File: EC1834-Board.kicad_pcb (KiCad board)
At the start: 2 copper layers, 18 parts

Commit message: Page 1 & 2 connected Hierarchival connections created and tested
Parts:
- moved REF** 103.7 mm to (22.2, -75.7)
- moved REF** 103.7 mm to (108.6, -47.8)
- moved REF** 103.7 mm to (54.6, -47.8)
- moved REF** 103.7 mm to (43.8, -47.8)
- moved REF** 103.7 mm to (22.2, -47.8)
- moved REF** 103.7 mm to (65.4, -47.8)
- moved REF** 103.7 mm to (87.0, -47.8)
- moved REF** 103.7 mm to (97.8, -47.8)
- moved REF** 103.7 mm to (33.0, -47.8)
- moved REF** 103.7 mm to (76.2, -47.8)
- moved REF** 103.7 mm to (33.0, -75.7)
- moved REF** 103.7 mm to (43.8, -75.7)
- moved REF** 103.7 mm to (54.6, -75.7)
- moved REF** 103.7 mm to (97.8, -75.7)
- moved REF** 103.7 mm to (87.0, -75.7)
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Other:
- board outline added: 360 x 240 mm
- copper layers 2 -> 6
- net class Default removed

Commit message: Updated footprint for EMR UC8821 Added footprint for PS5 PCB layout in progress small corrections in schematics
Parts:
- added BR1: SolderJumper_2_Bridged, Resistor_THT:R_Axial_DIN0204_L3.6mm_D1.6mm_P7.62mm_Horizontal, F.Cu at (259.1, -55.9)
- added Br2: Br2, Resistor_THT:R_Axial_DIN0204_L3.6mm_D1.6mm_P7.62mm_Horizontal, F.Cu at (362.2, -28.5)
- added Br3: Br3, Resistor_THT:R_Axial_DIN0204_L3.6mm_D1.6mm_P7.62mm_Horizontal, F.Cu at (362.2, -31.7)
- added Br4: Br4, Resistor_THT:R_Axial_DIN0204_L3.6mm_D1.6mm_P5.08mm_Horizontal, F.Cu at (251.4, -191.6)
- added C10: 10pF, Capacitor_THT:C_Disc_D4.3mm_W1.9mm_P5.00mm, F.Cu at (184.2, -131.2)
- added C101: 47µF, Capacitor_THT:CP_Radial_D12.5mm_P5.00mm, F.Cu at (521.1, -90.7)
- added C102: 47µF, Capacitor_THT:CP_Radial_D12.5mm_P5.00mm, F.Cu at (564.3, -79.0)
- added C103: 47µF, Capacitor_THT:CP_Radial_D12.5mm_P5.00mm, F.Cu at (536.9, -95.4)
- added C104: 47µF, Capacitor_THT:CP_Radial_D12.5mm_P5.00mm, F.Cu at (551.3, -95.4)
- added C105: 47µF, Capacitor_THT:CP_Radial_D12.5mm_P5.00mm, F.Cu at (608.4, -121.2)
- added C106: 47µF, Capacitor_THT:CP_Radial_D12.5mm_P5.00mm, F.Cu at (594.0, -121.2)
- added C107: 47µF, Capacitor_THT:CP_Radial_D12.5mm_P5.00mm, F.Cu at (535.5, -67.3)
- added C108: 47µF, Capacitor_THT:CP_Radial_D12.5mm_P5.00mm, F.Cu at (594.5, -93.1)
- added C109: 47µF, Capacitor_THT:CP_Radial_D12.5mm_P5.00mm, F.Cu at (580.1, -93.1)
- added C110: 47µF, Capacitor_THT:CP_Radial_D12.5mm_P5.00mm, F.Cu at (593.1, -79.0)
- added C111: 47µF, Capacitor_THT:CP_Radial_D12.5mm_P5.00mm, F.Cu at (598.3, -107.1)
- added C112: 47µF, Capacitor_THT:CP_Radial_D12.5mm_P5.00mm, F.Cu at (637.2, -121.2)
- added C113: 47µF, Capacitor_THT:CP_Radial_D12.5mm_P5.00mm, F.Cu at (578.7, -79.0)
- added C114: 47µF, Capacitor_THT:CP_Radial_D12.5mm_P5.00mm, F.Cu at (583.9, -107.1)
- added C115: 47µF, Capacitor_THT:CP_Radial_D12.5mm_P5.00mm, F.Cu at (549.9, -67.3)
- added C116: 47µF, Capacitor_THT:CP_Radial_D12.5mm_P5.00mm, F.Cu at (579.6, -121.2)
- added C117: 47µF, Capacitor_THT:CP_Radial_D12.5mm_P5.00mm, F.Cu at (578.7, -65.0)
- added C118: 47µF, Capacitor_THT:CP_Radial_D12.5mm_P5.00mm, F.Cu at (549.9, -81.4)
- added C119: 47µF, Capacitor_THT:CP_Radial_D12.5mm_P5.00mm, F.Cu at (565.7, -93.1)
- added C120: 47µF, Capacitor_THT:CP_Radial_D12.5mm_P5.00mm, F.Cu at (521.1, -62.6)
- added C121: 47µF, Capacitor_THT:CP_Radial_D12.5mm_P5.00mm, F.Cu at (535.5, -81.4)
- added C122: 47µF, Capacitor_THT:CP_Radial_D12.5mm_P5.00mm, F.Cu at (564.3, -65.0)
- added C123: 47µF, Capacitor_THT:CP_Radial_D12.5mm_P5.00mm, F.Cu at (569.5, -107.1)
- added C2: 47µF, Capacitor_THT:CP_Radial_D12.5mm_P5.00mm, F.Cu at (622.8, -121.2)
- added C3: 47µF, Capacitor_THT:CP_Radial_D12.5mm_P5.00mm, F.Cu at (342.3, 231.8)
- added C4: 47µF, Capacitor_THT:CP_Radial_D12.5mm_P5.00mm, F.Cu at (521.1, -76.6)
- added C5: 47µF, Capacitor_THT:CP_Radial_D12.5mm_P5.00mm, F.Cu at (286.4, -149.8)
- added C6: 10nF, Capacitor_THT:C_Disc_D4.3mm_W1.9mm_P5.00mm, F.Cu at (185.4, -145.8)
- added C7: 680pF, Capacitor_THT:C_Disc_D4.3mm_W1.9mm_P5.00mm, F.Cu at (266.7, -87.0)
- added C8: 680pF, Capacitor_THT:C_Disc_D4.3mm_W1.9mm_P5.00mm, F.Cu at (221.7, -30.8)
- added D1: K1810WM87, Package_DIP:DIP-40_W15.24mm, F.Cu at (347.3, 208.3)
- added D10: DL000D, Package_DIP:DIP-14_W7.62mm, F.Cu at (170.4, 219.1)
- added D100: U2764, Package_DIP:DIP-28_W15.24mm, F.Cu at (185.4, 31.1)
- added D101: U2764, Package_DIP:DIP-28_W15.24mm, F.Cu at (144.8, 31.1)
- added D102: U2164, Package_DIP:DIP-16_W7.62mm, F.Cu at (106.7, 55.2)
- added D103: U2164, Package_DIP:DIP-16_W7.62mm, F.Cu at (96.5, 55.2)
- added D104: U2164, Package_DIP:DIP-16_W7.62mm, F.Cu at (86.3, 55.2)
- added D105: U2164, Package_DIP:DIP-16_W7.62mm, F.Cu at (76.2, 55.2)
- added D106: U2164, Package_DIP:DIP-16_W7.62mm, F.Cu at (66.0, 55.2)
- added D107: U2164, Package_DIP:DIP-16_W7.62mm, F.Cu at (55.9, 55.2)
- added D108: U2164, Package_DIP:DIP-16_W7.62mm, F.Cu at (45.7, 55.2)
- added D109: U2164, Package_DIP:DIP-16_W7.62mm, F.Cu at (35.5, 55.2)
- added D11: DL020D, Package_DIP:DIP-14_W7.62mm, F.Cu at (158.3, 219.1)
- added D110: U2164, Package_DIP:DIP-16_W7.62mm, F.Cu at (25.4, 55.2)
- added D111: DS8286D-D111, Package_DIP:DIP-20_W7.62mm, F.Cu at (244.5, 33.6)
- added D112: DS8286D-D111, Package_DIP:DIP-20_W7.62mm, F.Cu at (229.9, 33.7)
- added D113: KR531IP5, Package_DIP:DIP-14_W7.62mm, F.Cu at (215.3, 33.7)
- added D114: KR531IP5, Package_DIP:DIP-14_W7.62mm, F.Cu at (202.6, 33.7)
- added D115: U2764, Package_DIP:DIP-28_W15.24mm, F.Cu at (185.4, 10.8)
- added D116: U2764, Package_DIP:DIP-28_W15.24mm, F.Cu at (144.8, 10.8)
- added D117: U2164, Package_DIP:DIP-16_W7.62mm, F.Cu at (106.7, 28.6)
- added D118: U2164, Package_DIP:DIP-16_W7.62mm, F.Cu at (96.5, 28.6)
- added D119: U2164, Package_DIP:DIP-16_W7.62mm, F.Cu at (86.3, 28.6)
- added D12: DL008D, Package_DIP:DIP-14_W7.62mm, F.Cu at (146.3, 219.1)
- added D120: U2164, Package_DIP:DIP-16_W7.62mm, F.Cu at (76.2, 28.6)
- added D121: U2164, Package_DIP:DIP-16_W7.62mm, F.Cu at (66.0, 28.6)
- added D122: U2164, Package_DIP:DIP-16_W7.62mm, F.Cu at (55.9, 28.6)
- added D123: U2164, Package_DIP:DIP-16_W7.62mm, F.Cu at (45.7, 28.6)
- added D124: U2164, Package_DIP:DIP-16_W7.62mm, F.Cu at (35.5, 28.6)
- added D125: U2164, Package_DIP:DIP-16_W7.62mm, F.Cu at (25.4, 28.6)
- added D126: DL074, Package_DIP:DIP-14_W7.62mm, F.Cu at (354.3, 64.1)
- added D13: DL074, Package_DIP:DIP-14_W7.62mm, F.Cu at (134.2, 219.1)
- added D14: DL010D, Package_DIP:DIP-14_W7.62mm, F.Cu at (119.6, 219.1)
- added D15: DL074, Package_DIP:DIP-14_W7.62mm, F.Cu at (105.0, 219.1)
- added D16: DL000D, Package_DIP:DIP-14_W7.62mm, F.Cu at (89.5, 219.1)
- added D2: DS8282, Package_DIP:DIP-20_W7.62mm, F.Cu at (285.1, 218.4)
- added D20: K1810WM86, Package_DIP:DIP-40_W15.24mm, F.Cu at (342.3, 188.0)
- added D21: DS8286D-D111, Package_DIP:DIP-20_W7.62mm, F.Cu at (339.7, 182.9)
- added D22: DS8286D, Package_DIP:DIP-20_W7.62mm, F.Cu at (327.0, 182.9)
- added D23: DS8286D-D23, Package_DIP:DIP-20_W7.62mm, F.Cu at (314.3, 182.9)
- added D24: DL374, Package_DIP:DIP-20_W7.62mm, F.Cu at (301.6, 182.9)
- added D25: DS8282, Package_DIP:DIP-20_W7.62mm, F.Cu at (285.1, 185.4)
- added D26: DS8282, Package_DIP:DIP-20_W7.62mm, F.Cu at (272.4, 185.4)
- added D27: DS8286D-D27, Package_DIP:DIP-20_W7.62mm, F.Cu at (244.5, 185.2)
- added D28: DL295, Package_DIP:DIP-14_W7.62mm, F.Cu at (228.0, 198.2)
- added D29: DL295, Package_DIP:DIP-14_W7.62mm, F.Cu at (228.0, 177.9)
- added D3: DL020D, Package_DIP:DIP-14_W7.62mm, F.Cu at (272.4, 218.4)
- added D30: DL374, Package_DIP:DIP-20_W7.62mm, F.Cu at (215.3, 185.5)
- added D31: DL374, Package_DIP:DIP-20_W7.62mm, F.Cu at (202.6, 185.5)
- added D32: DL000D, Package_DIP:DIP-14_W7.62mm, F.Cu at (182.5, 193.7)
- added D33: DL002D, Package_DIP:DIP-14_W7.62mm, F.Cu at (170.2, 193.7)
- added D34: DL004D, Package_DIP:DIP-14_W7.62mm, F.Cu at (158.1, 193.7)
- added D35: DL175, Package_DIP:DIP-16_W7.62mm, F.Cu at (146.1, 193.7)
- added D36: DL175, Package_DIP:DIP-16_W7.62mm, F.Cu at (134.0, 193.7)
- added D37: DL032D, Package_DIP:DIP-14_W7.62mm, F.Cu at (119.4, 193.7)
- added D38: DL074, Package_DIP:DIP-14_W7.62mm, F.Cu at (104.8, 193.7)
- added D39: DL000D, Package_DIP:DIP-14_W7.62mm, F.Cu at (89.5, 193.7)
- added D4: KR1810WG88, Package_DIP:DIP-20_W7.62mm, F.Cu at (259.7, 218.4)
- added D40: DL008D, Package_DIP:DIP-14_W7.62mm, F.Cu at (74.9, 193.7)
- added D42: A302D, Package_DIP:DIP-4_W7.62mm, F.Cu at (185.5, -165.0)
- added D43: 8284, Package_DIP:DIP-18_W7.62mm, F.Cu at (356.9, 139.7)
- added D44: DS8286D-D111, Package_DIP:DIP-20_W7.62mm, F.Cu at (244.5, 151.1)
- added D45: DS8282, Package_DIP:DIP-20_W7.62mm, F.Cu at (228.0, 151.1)
- added D46: DS8216, Package_DIP:DIP-16_W7.62mm, F.Cu at (215.3, 146.0)
- added D47: DL008D, Package_DIP:DIP-14_W7.62mm, F.Cu at (202.6, 143.5)
- added D48: KR580WN59A, Package_DIP:DIP-28_W15.24mm, F.Cu at (185.4, 165.1)
- added D49: KR580WN59A, Package_DIP:DIP-28_W15.24mm, F.Cu at (165.7, 165.1)
- added D5: DL030D, Package_DIP:DIP-14_W7.62mm, F.Cu at (244.5, 218.4)
- added D50: KR580IK57, Package_DIP:DIP-40_W15.24mm, F.Cu at (146.0, 165.1)
- added D51: DL074, Package_DIP:DIP-14_W7.62mm, F.Cu at (121.9, 165.1)
- added D52: 74HC74, Package_DIP:DIP-14_W7.62mm, F.Cu at (121.9, 139.7)
- added D53: KR580WI53, Package_DIP:DIP-24_W15.24mm, F.Cu at (106.7, 144.8)
- added D54: 8255A, Package_DIP:DIP-40_W15.24mm, F.Cu at (83.2, 165.1)
- added D55: UC8821, EC1834-Board:EMR-64_W22.86mm, F.Cu at (61.0, 156.2)
- added D56: 2716, Package_DIP:DIP-24_W15.24mm, F.Cu at (30.5, 147.3)
- added D57: DL008D, Package_DIP:DIP-14_W7.62mm, F.Cu at (244.5, 123.2)
- added D58: 74HC74, Package_DIP:DIP-14_W7.62mm, F.Cu at (228.0, 123.2)
- added D59: DL004D, Package_DIP:DIP-14_W7.62mm, F.Cu at (215.3, 123.2)
- added D6: DL295, Package_DIP:DIP-14_W7.62mm, F.Cu at (228.0, 218.4)
- added D60: 74HC74, Package_DIP:DIP-14_W7.62mm, F.Cu at (202.6, 123.2)
- added D61: DS8216, Package_DIP:DIP-16_W7.62mm, F.Cu at (185.4, 123.2)
- added D62: DL032D, Package_DIP:DIP-14_W7.62mm, F.Cu at (173.4, 123.2)
- added D63: DL010D-D63, Package_DIP:DIP-14_W7.62mm, F.Cu at (160.0, 123.2)
- added D64: DS8286D-D23, Package_DIP:DIP-20_W7.62mm, F.Cu at (244.5, 99.0)
- added D65: DS8205, Package_DIP:DIP-16_W7.62mm, F.Cu at (228.0, 99.0)
- added D66: DS8205, Package_DIP:DIP-16_W7.62mm, F.Cu at (215.3, 99.0)
- added D67: DL074, Package_DIP:DIP-14_W7.62mm, F.Cu at (202.6, 99.1)
- added D68: 74S51, Package_DIP:DIP-14_W7.62mm, F.Cu at (185.4, 99.1)
- added D69: DL008D, Package_DIP:DIP-14_W7.62mm, F.Cu at (173.3, 99.1)
- added D7: DL032D, Package_DIP:DIP-14_W7.62mm, F.Cu at (215.2, 218.4)
- added D70: DL008D, Package_DIP:DIP-14_W7.62mm, F.Cu at (160.0, 99.1)
- added D71: DL002D, Package_DIP:DIP-14_W7.62mm, F.Cu at (138.4, 106.7)
- added D72: DL008D, Package_DIP:DIP-14_W7.62mm, F.Cu at (121.9, 109.2)
- added D73: U2164, Package_DIP:DIP-16_W7.62mm, F.Cu at (106.7, 107.9)
- added D74: U2164, Package_DIP:DIP-16_W7.62mm, F.Cu at (96.5, 107.9)
- added D75: U2164, Package_DIP:DIP-16_W7.62mm, F.Cu at (86.3, 107.9)
- added D76: U2164, Package_DIP:DIP-16_W7.62mm, F.Cu at (76.2, 107.9)
- added D77: U2164, Package_DIP:DIP-16_W7.62mm, F.Cu at (66.0, 107.9)
- added D78: U2164, Package_DIP:DIP-16_W7.62mm, F.Cu at (55.9, 107.9)
- added D79: U2164, Package_DIP:DIP-16_W7.62mm, F.Cu at (45.7, 107.9)
- added D8: DL004D, Package_DIP:DIP-14_W7.62mm, F.Cu at (202.5, 218.4)
- added D80: U2164, Package_DIP:DIP-16_W7.62mm, F.Cu at (35.5, 107.9)
- added D81: U2164, Package_DIP:DIP-16_W7.62mm, F.Cu at (25.4, 107.9)
- added D82: DL004D, Package_DIP:DIP-14_W7.62mm, F.Cu at (11.4, 99.7)
- added D83: DS8286D, Package_DIP:DIP-20_W7.62mm, F.Cu at (244.5, 66.7)
- added D84: DS8286D, Package_DIP:DIP-20_W7.62mm, F.Cu at (228.0, 66.7)
- added D85: KR531KP11, Package_DIP:DIP-16_W7.62mm, F.Cu at (215.3, 61.6)
- added D86: KR531KP11, Package_DIP:DIP-16_W7.62mm, F.Cu at (202.6, 61.6)
- added D87: DL004D, Package_DIP:DIP-14_W7.62mm, F.Cu at (173.3, 73.0)
- added D88: DL008D, Package_DIP:DIP-14_W7.62mm, F.Cu at (160.0, 73.0)
- added D89: DS8205, Package_DIP:DIP-16_W7.62mm, F.Cu at (138.4, 73.0)
- added D9: DS8205, Package_DIP:DIP-16_W7.62mm, F.Cu at (182.5, 219.1)
- added D90: KR531LI1, Package_DIP:DIP-14_W7.62mm, F.Cu at (123.8, 73.0)
- added D91: U2164, Package_DIP:DIP-16_W7.62mm, F.Cu at (106.7, 81.9)
- added D92: U2164, Package_DIP:DIP-16_W7.62mm, F.Cu at (96.5, 81.9)
- added D93: U2164, Package_DIP:DIP-16_W7.62mm, F.Cu at (86.3, 81.9)
- added D94: U2164, Package_DIP:DIP-16_W7.62mm, F.Cu at (76.2, 81.9)
- added D95: U2164, Package_DIP:DIP-16_W7.62mm, F.Cu at (66.0, 81.9)
- added D96: U2164, Package_DIP:DIP-16_W7.62mm, F.Cu at (55.9, 81.9)
- added D97: U2164, Package_DIP:DIP-16_W7.62mm, F.Cu at (45.7, 81.9)
- added D98: U2164, Package_DIP:DIP-16_W7.62mm, F.Cu at (35.5, 81.9)
- added D99: U2164, Package_DIP:DIP-16_W7.62mm, F.Cu at (25.4, 81.9)
- added E1: SolderJumper_2_Bridged, Connector_PinHeader_2.54mm:PinHeader_1x02_P2.54mm_Vertical, F.Cu at (284.8, -239.8)
- added E2: SolderJumper_2_Bridged, Connector_PinHeader_2.54mm:PinHeader_1x02_P2.54mm_Vertical, F.Cu at (343.7, -215.2)
- added E4: SolderJumper_2_Bridged, Connector_PinHeader_2.54mm:PinHeader_1x02_P2.54mm_Vertical, F.Cu at (44.5, 167.0)
- added E5: SolderJumper_2_Bridged, Connector_PinHeader_2.54mm:PinHeader_1x02_P2.54mm_Vertical, F.Cu at (284.8, -232.6)
- added E6: Conn_01x02, Connector_PinHeader_2.54mm:PinHeader_1x02_P2.54mm_Vertical, F.Cu at (649.0, -111.5)
- added E7: Conn_01x02, Connector_PinHeader_2.54mm:PinHeader_1x02_P2.54mm_Vertical, F.Cu at (649.0, -104.3)
- added E8: Conn_01x02, Connector_PinHeader_2.54mm:PinHeader_1x02_P2.54mm_Vertical, F.Cu at (649.1, -118.7)
- added K1: 100n, Capacitor_THT:C_Disc_D4.3mm_W1.9mm_P5.00mm, F.Cu at (638.2, -95.2)
- added K10: 100n, Capacitor_THT:C_Disc_D4.3mm_W1.9mm_P5.00mm, F.Cu at (583.0, -56.2)
- added K100: 100n, Capacitor_THT:C_Disc_D4.3mm_W1.9mm_P5.00mm, F.Cu at (525.9, -50.4)
- added K101: 100n, Capacitor_THT:C_Disc_D4.3mm_W1.9mm_P5.00mm, F.Cu at (534.1, -55.1)
- added K102: 100n, Capacitor_THT:C_Disc_D4.3mm_W1.9mm_P5.00mm, F.Cu at (607.4, -53.3)
- added K103: 100n, Capacitor_THT:C_Disc_D4.3mm_W1.9mm_P5.00mm, F.Cu at (628.6, -74.5)
- added K104: 100n, Capacitor_THT:C_Disc_D4.3mm_W1.9mm_P5.00mm, F.Cu at (589.8, -66.8)
- added K105: 100n, Capacitor_THT:C_Disc_D4.3mm_W1.9mm_P5.00mm, F.Cu at (615.6, -57.0)
- added K106: 100n, Capacitor_THT:C_Disc_D4.3mm_W1.9mm_P5.00mm, F.Cu at (607.4, -49.8)
- added K107: 100n, Capacitor_THT:C_Disc_D4.3mm_W1.9mm_P5.00mm, F.Cu at (636.8, -81.4)
- added K108: 100n, Capacitor_THT:C_Disc_D4.3mm_W1.9mm_P5.00mm, F.Cu at (622.4, -63.9)
- added K109: 100n, Capacitor_THT:C_Disc_D4.3mm_W1.9mm_P5.00mm, F.Cu at (630.5, -71.0)
- added K11: 100n, Capacitor_THT:C_Disc_D4.3mm_W1.9mm_P5.00mm, F.Cu at (605.6, -94.9)
- added K110: 100n, Capacitor_THT:C_Disc_D4.3mm_W1.9mm_P5.00mm, F.Cu at (636.8, -77.9)
- added K111: 100n, Capacitor_THT:C_Disc_D4.3mm_W1.9mm_P5.00mm, F.Cu at (591.1, -53.0)
- added K112: 100n, Capacitor_THT:C_Disc_D4.3mm_W1.9mm_P5.00mm, F.Cu at (612.3, -74.2)
- added K113: 100n, Capacitor_THT:C_Disc_D4.3mm_W1.9mm_P5.00mm, F.Cu at (534.1, -51.7)
- added K114: 100n, Capacitor_THT:C_Disc_D4.3mm_W1.9mm_P5.00mm, F.Cu at (534.1, -48.2)
- added K115: 100n, Capacitor_THT:C_Disc_D4.3mm_W1.9mm_P5.00mm, F.Cu at (540.3, -58.6)
- added K116: 100n, Capacitor_THT:C_Disc_D4.3mm_W1.9mm_P5.00mm, F.Cu at (542.2, -55.1)
- added K117: 100n, Capacitor_THT:C_Disc_D4.3mm_W1.9mm_P5.00mm, F.Cu at (615.6, -53.5)
- added K118: 100n, Capacitor_THT:C_Disc_D4.3mm_W1.9mm_P5.00mm, F.Cu at (636.8, -74.5)
- added K119: 100n, Capacitor_THT:C_Disc_D4.3mm_W1.9mm_P5.00mm, F.Cu at (623.7, -57.0)
- added K12: 100n, Capacitor_THT:C_Disc_D4.3mm_W1.9mm_P5.00mm, F.Cu at (631.9, -109.0)
- added K120: 100n, Capacitor_THT:C_Disc_D4.3mm_W1.9mm_P5.00mm, F.Cu at (615.6, -50.1)
- added K121: 100n, Capacitor_THT:C_Disc_D4.3mm_W1.9mm_P5.00mm, F.Cu at (630.5, -67.6)
- added K122: 100n, Capacitor_THT:C_Disc_D4.3mm_W1.9mm_P5.00mm, F.Cu at (542.2, -51.7)
- added K123: 100n, Capacitor_THT:C_Disc_D4.3mm_W1.9mm_P5.00mm, F.Cu at (548.5, -58.6)
- added K124: 100n, Capacitor_THT:C_Disc_D4.3mm_W1.9mm_P5.00mm, F.Cu at (542.2, -48.2)
- added K125: 100n, Capacitor_THT:C_Disc_D4.3mm_W1.9mm_P5.00mm, F.Cu at (550.4, -55.1)
- added K126: 100n, Capacitor_THT:C_Disc_D4.3mm_W1.9mm_P5.00mm, F.Cu at (589.8, -59.9)
- added K13: 100n, Capacitor_THT:C_Disc_D4.3mm_W1.9mm_P5.00mm, F.Cu at (640.1, -112.4)
- added K14: 100n, Capacitor_THT:C_Disc_D4.3mm_W1.9mm_P5.00mm, F.Cu at (591.1, -56.5)
- added K15: 100n, Capacitor_THT:C_Disc_D4.3mm_W1.9mm_P5.00mm, F.Cu at (621.9, -95.2)
- added K16: 100n, Capacitor_THT:C_Disc_D4.3mm_W1.9mm_P5.00mm, F.Cu at (574.8, -49.3)
- added K18: 100n, Capacitor_THT:C_Disc_D4.3mm_W1.9mm_P5.00mm, F.Cu at (622.4, -67.3)
- added K19: 100n, Capacitor_THT:C_Disc_D4.3mm_W1.9mm_P5.00mm, F.Cu at (622.4, -60.4)
- added K2: 100n, Capacitor_THT:C_Disc_D4.3mm_W1.9mm_P5.00mm, F.Cu at (280.7, 223.5)
- added K21: 100n, Capacitor_THT:C_Disc_D4.3mm_W1.9mm_P5.00mm, F.Cu at (583.0, -49.3)
- added K22: 100n, Capacitor_THT:C_Disc_D4.3mm_W1.9mm_P5.00mm, F.Cu at (631.9, -98.6)
- added K23: 100n, Capacitor_THT:C_Disc_D4.3mm_W1.9mm_P5.00mm, F.Cu at (640.1, -109.0)
- added K24: 100n, Capacitor_THT:C_Disc_D4.3mm_W1.9mm_P5.00mm, F.Cu at (597.9, -66.8)
- added K25: 100n, Capacitor_THT:C_Disc_D4.3mm_W1.9mm_P5.00mm, F.Cu at (278.1, 190.5)
- added K26: 100n, Capacitor_THT:C_Disc_D4.3mm_W1.9mm_P5.00mm, F.Cu at (550.4, -48.2)
- added K27: 100n, Capacitor_THT:C_Disc_D4.3mm_W1.9mm_P5.00mm, F.Cu at (606.1, -70.5)
- added K28: 100n, Capacitor_THT:C_Disc_D4.3mm_W1.9mm_P5.00mm, F.Cu at (574.8, -56.2)
- added K29: 100n, Capacitor_THT:C_Disc_D4.3mm_W1.9mm_P5.00mm, F.Cu at (623.8, -109.0)
- added K3: 100n, Capacitor_THT:C_Disc_D4.3mm_W1.9mm_P5.00mm, F.Cu at (605.6, -98.4)
- added K30: 100n, Capacitor_THT:C_Disc_D4.3mm_W1.9mm_P5.00mm, F.Cu at (212.6, 190.5)
- added K31: 100n, Capacitor_THT:C_Disc_D4.3mm_W1.9mm_P5.00mm, F.Cu at (199.9, 190.5)
- added K32: 100n, Capacitor_THT:C_Disc_D4.3mm_W1.9mm_P5.00mm, F.Cu at (670.6, -94.0)
- added K33: 100n, Capacitor_THT:C_Disc_D4.3mm_W1.9mm_P5.00mm, F.Cu at (597.9, -63.4)
- added K34: 100n, Capacitor_THT:C_Disc_D4.3mm_W1.9mm_P5.00mm, F.Cu at (605.6, -91.5)
- added K35: 100n, Capacitor_THT:C_Disc_D4.3mm_W1.9mm_P5.00mm, F.Cu at (630.1, -95.2)
- added K36: 100n, Capacitor_THT:C_Disc_D4.3mm_W1.9mm_P5.00mm, F.Cu at (620.5, -84.6)
- added K37: 100n, Capacitor_THT:C_Disc_D4.3mm_W1.9mm_P5.00mm, F.Cu at (566.7, -52.8)
- added K38: 100n, Capacitor_THT:C_Disc_D4.3mm_W1.9mm_P5.00mm, F.Cu at (612.3, -84.6)
- added K39: 100n, Capacitor_THT:C_Disc_D4.3mm_W1.9mm_P5.00mm, F.Cu at (604.2, -80.9)
- added K4: 100n, Capacitor_THT:C_Disc_D4.3mm_W1.9mm_P5.00mm, F.Cu at (558.5, -49.3)
- added K40: 100n, Capacitor_THT:C_Disc_D4.3mm_W1.9mm_P5.00mm, F.Cu at (613.8, -91.5)
- added K43: 100n, Capacitor_THT:C_Disc_D4.3mm_W1.9mm_P5.00mm, F.Cu at (630.1, -91.7)
- added K44: 100n, Capacitor_THT:C_Disc_D4.3mm_W1.9mm_P5.00mm, F.Cu at (238.1, 156.2)
- added K45: 100n, Capacitor_THT:C_Disc_D4.3mm_W1.9mm_P5.00mm, F.Cu at (558.5, -52.8)
- added K46: 100n, Capacitor_THT:C_Disc_D4.3mm_W1.9mm_P5.00mm, F.Cu at (597.9, -59.9)
- added K47: 100n, Capacitor_THT:C_Disc_D4.3mm_W1.9mm_P5.00mm, F.Cu at (636.8, -84.8)
- added K48: 100n, Capacitor_THT:C_Disc_D4.3mm_W1.9mm_P5.00mm, F.Cu at (591.1, -49.6)
- added K49: 100n, Capacitor_THT:C_Disc_D4.3mm_W1.9mm_P5.00mm, F.Cu at (640.1, -98.6)
- added K5: 100n, Capacitor_THT:C_Disc_D4.3mm_W1.9mm_P5.00mm, F.Cu at (566.7, -56.2)
- added K50: 100n, Capacitor_THT:C_Disc_D4.3mm_W1.9mm_P5.00mm, F.Cu at (620.5, -81.1)
- added K51: 100n, Capacitor_THT:C_Disc_D4.3mm_W1.9mm_P5.00mm, F.Cu at (631.9, -102.1)
- added K52: 100n, Capacitor_THT:C_Disc_D4.3mm_W1.9mm_P5.00mm, F.Cu at (630.5, -64.1)
- added K53: 100n, Capacitor_THT:C_Disc_D4.3mm_W1.9mm_P5.00mm, F.Cu at (550.3, -111.2)
- added K54: 100n, Capacitor_THT:C_Disc_D4.3mm_W1.9mm_P5.00mm, F.Cu at (566.2, -117.0)
- added K55: 100n, Capacitor_THT:C_Disc_D4.3mm_W1.9mm_P5.00mm, F.Cu at (620.5, -74.2)
- added K56: 100n, Capacitor_THT:C_Disc_D4.3mm_W1.9mm_P5.00mm, F.Cu at (557.6, -107.8)
- added K57: 100n, Capacitor_THT:C_Disc_D4.3mm_W1.9mm_P5.00mm, F.Cu at (239.4, 104.8)
- added K58: 100n, Capacitor_THT:C_Disc_D4.3mm_W1.9mm_P5.00mm, F.Cu at (638.7, -71.0)
- added K59: 100n, Capacitor_THT:C_Disc_D4.3mm_W1.9mm_P5.00mm, F.Cu at (605.6, -88.0)
- added K6: 100n, Capacitor_THT:C_Disc_D4.3mm_W1.9mm_P5.00mm, F.Cu at (623.8, -112.4)
- added K60: 100n, Capacitor_THT:C_Disc_D4.3mm_W1.9mm_P5.00mm, F.Cu at (549.5, -105.5)
- added K61: 100n, Capacitor_THT:C_Disc_D4.3mm_W1.9mm_P5.00mm, F.Cu at (599.3, -56.5)
- added K62: 100n, Capacitor_THT:C_Disc_D4.3mm_W1.9mm_P5.00mm, F.Cu at (566.7, -49.3)
- added K63: 100n, Capacitor_THT:C_Disc_D4.3mm_W1.9mm_P5.00mm, F.Cu at (557.6, -104.3)
- added K64: 100n, Capacitor_THT:C_Disc_D4.3mm_W1.9mm_P5.00mm, F.Cu at (604.2, -74.0)
- added K65: 100n, Capacitor_THT:C_Disc_D4.3mm_W1.9mm_P5.00mm, F.Cu at (604.2, -84.3)
- added K66: 100n, Capacitor_THT:C_Disc_D4.3mm_W1.9mm_P5.00mm, F.Cu at (623.8, -102.1)
- added K67: 100n, Capacitor_THT:C_Disc_D4.3mm_W1.9mm_P5.00mm, F.Cu at (583.0, -52.8)
- added K68: 100n, Capacitor_THT:C_Disc_D4.3mm_W1.9mm_P5.00mm, F.Cu at (517.8, -53.8)
- added K69: 100n, Capacitor_THT:C_Disc_D4.3mm_W1.9mm_P5.00mm, F.Cu at (631.9, -105.5)
- added K7: 100n, Capacitor_THT:C_Disc_D4.3mm_W1.9mm_P5.00mm, F.Cu at (623.8, -105.5)
- added K70: 100n, Capacitor_THT:C_Disc_D4.3mm_W1.9mm_P5.00mm, F.Cu at (597.9, -70.3)
- added K71: 100n, Capacitor_THT:C_Disc_D4.3mm_W1.9mm_P5.00mm, F.Cu at (612.3, -77.7)
- added K72: 100n, Capacitor_THT:C_Disc_D4.3mm_W1.9mm_P5.00mm, F.Cu at (589.8, -63.4)
- added K73: 100n, Capacitor_THT:C_Disc_D4.3mm_W1.9mm_P5.00mm, F.Cu at (606.1, -67.1)
- added K74: 100n, Capacitor_THT:C_Disc_D4.3mm_W1.9mm_P5.00mm, F.Cu at (630.1, -88.3)
- added K75: 100n, Capacitor_THT:C_Disc_D4.3mm_W1.9mm_P5.00mm, F.Cu at (606.1, -63.6)
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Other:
- board size 360 x 240 mm -> 378.5 x 240 mm

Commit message: Updated footprints Updated PCB
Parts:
- C5: footprint Capacitor_THT:CP_Radial_D12.5mm_P5.00mm -> Capacitor_THT:CP_Axial_L18.0mm_D6.5mm_P25.00mm_Horizontal
- R1, R13, R17, R18, R19, R2, R20, R21, R22, R24, R25, R3, R30, R31, R32, R33, R4, R5, R50, R51, R53, R54, R6, R7, R8: footprint Resistor_THT:R_Axial_DIN0309_L9.0mm_D3.2mm_P12.70mm_Horizontal -> EC1834-Board:R_Axial_L9.0mm_D1.8mm_P12.70mm_Horizontal
- moved X5 721.8 mm to (6.98, 203.8), turned to 90 degrees
- moved E6 707.9 mm to (29.8, 231.8)
- moved R22 648.5 mm to (12.7, 226.1), turned to 90 degrees
- moved V2 539.9 mm to (8.41, 189.2)
- moved E8 524.3 mm to (202.6, 156.2), turned to 90 degrees
- moved X6 513.4 mm to (5.71, 175.3), turned to 90 degrees
- moved E7 476.6 mm to (185.4, 6.35), turned to -90 degrees
- moved C5 440.5 mm to (23.5, 203.6), turned to 90 degrees
- moved X4 393.3 mm to (17.8, 224.2), turned to 90 degrees
- moved D42 389.8 mm to (13.3, 184.8), turned to 180 degrees
- moved C6 388.6 mm to (9.48, 200.7), turned to 180 degrees
- moved E1 381.9 mm to (346.1, 137.2)
- moved R1 377.2 mm to (354.3, 206.4), turned to -90 degrees
- moved E5 356.0 mm to (346.1, 118.1)
- moved E2 347.3 mm to (346.1, 132.1), turned to 180 degrees
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
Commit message: Completed PCB layout Changed PS5
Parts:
- removed C118, C122, C123: 47µF, Capacitor_THT:CP_Radial_D12.5mm_P5.00mm
- removed K114, K21, K26, K28, K29, K32, K35, K40, K43, K46, K47, K56, K67, K82, K85, K87: 100n, Capacitor_THT:C_Disc_D4.3mm_W1.9mm_P5.00mm
- removed PS5:1, PS5:10, PS5:11, PS5:12, PS5:13, PS5:14, PS5:15, PS5:16, PS5:17, PS5:18, PS5:19, PS5:2, PS5:20, PS5:21, PS5:22, PS5:23, PS5:24, PS5:25, PS5:26, PS5:27, PS5:28, PS5:3, PS5:4, PS5:5, PS5:6, PS5:7, PS5:8, PS5:9: PS5, EC1834-Board:Pruefstecker5_Single
- removed REF** (x18): DIP-18_W7.62mm, Package_DIP:DIP-18_W7.62mm
- added C127: 47µF, Capacitor_THT:CP_Radial_D5.0mm_P2.50mm, F.Cu at (36.8, 73.7)
- added K20: 100n, Capacitor_THT:C_Disc_D4.3mm_W1.9mm_P5.00mm, F.Cu at (375.3, 215.9)
- added PS5: PS5, EC1834-Board:Pruefstecker5, F.Cu at (100.3, 19.1)
- added RES2: DIP-16_W7.62mm, Package_DIP:DIP-16_W7.62mm, F.Cu at (102.9, 231.8)
- added RES3: DIP-16_W7.62mm, Package_DIP:DIP-16_W7.62mm, F.Cu at (87.0, 231.8)
- added RES4: DIP-16_W7.62mm, Package_DIP:DIP-16_W7.62mm, F.Cu at (72.4, 231.8)
- added RES6: DIP-20_W7.62mm, Package_DIP:DIP-20_W7.62mm, F.Cu at (87.0, 206.4)
- C101, C102, C103, C104, C105, C106, C107, C108, C109, C110, C111, C112, C113, C114, C115, C116, C117, C119, C120, C121, C2, C3, C4: footprint Capacitor_THT:CP_Radial_D12.5mm_P5.00mm -> Capacitor_THT:CP_Radial_D5.0mm_P2.50mm
- V3, V4, V5, V6: footprint LED_THT:LED_D5.0mm -> LED_THT:LED_D3.0mm
- moved K18 657.6 mm to (82.0, 236.2)
- moved K80 642.8 mm to (63.5, 125.1), turned to 180 degrees
- moved K55 638.6 mm to (85.7, 177.2), turned to 180 degrees
- moved K15 636.4 mm to (132.7, 236.2), turned to 180 degrees
- moved K109 630.1 mm to (63.5, 72.4), turned to 180 degrees
- moved K78 622.0 mm to (83.8, 125.1), turned to 180 degrees
- moved K97 617.8 mm to (73.7, 99.1), turned to 180 degrees
- moved K13 609.1 mm to (161.9, 236.2), turned to 180 degrees
- moved K19 606.9 mm to (67.3, 236.2)
- moved K93 602.5 mm to (114.3, 99.1), turned to 180 degrees
- moved K121 599.8 mm to (93.9, 45.7), turned to 180 degrees
- moved K9 597.5 mm to (205.2, 236.2)
- moved K12 594.3 mm to (173.9, 236.2), turned to 180 degrees
- moved K38 593.6 mm to (132.7, 211.5), turned to 180 degrees
- moved K76 587.4 mm to (104.1, 125.1), turned to 180 degrees
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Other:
- board size 378.5 x 240 mm -> 360 x 240 mm
- board text added: "E1 nur bei Einsatz von Schaltkreistyp 8284A bestücken 8284"

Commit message: Small optical changes
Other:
- board text added: "0V"
- board text added: "12N"
- board text added: "12P"
- board text added: "5N"
- board text added: "5P"
- board text added: "Optional Br4 geschl. wenn unbest."
- board text added: "PWR-LED"
- board text added: "RST"
- board text added: "SPK"

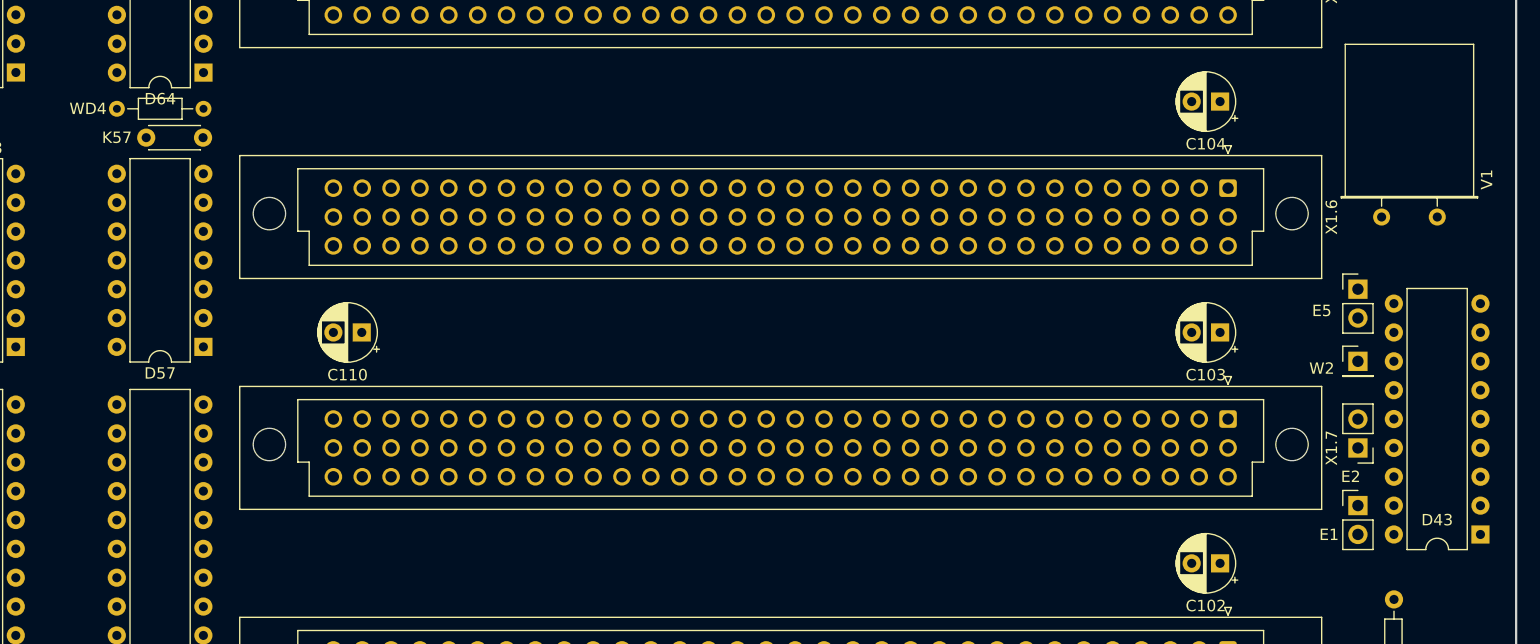
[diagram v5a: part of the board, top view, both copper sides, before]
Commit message: Updated some symbol pins no more error on PCB import due to leading zero on pin number also fixed missing network connections added unused pin connections on bus connectors
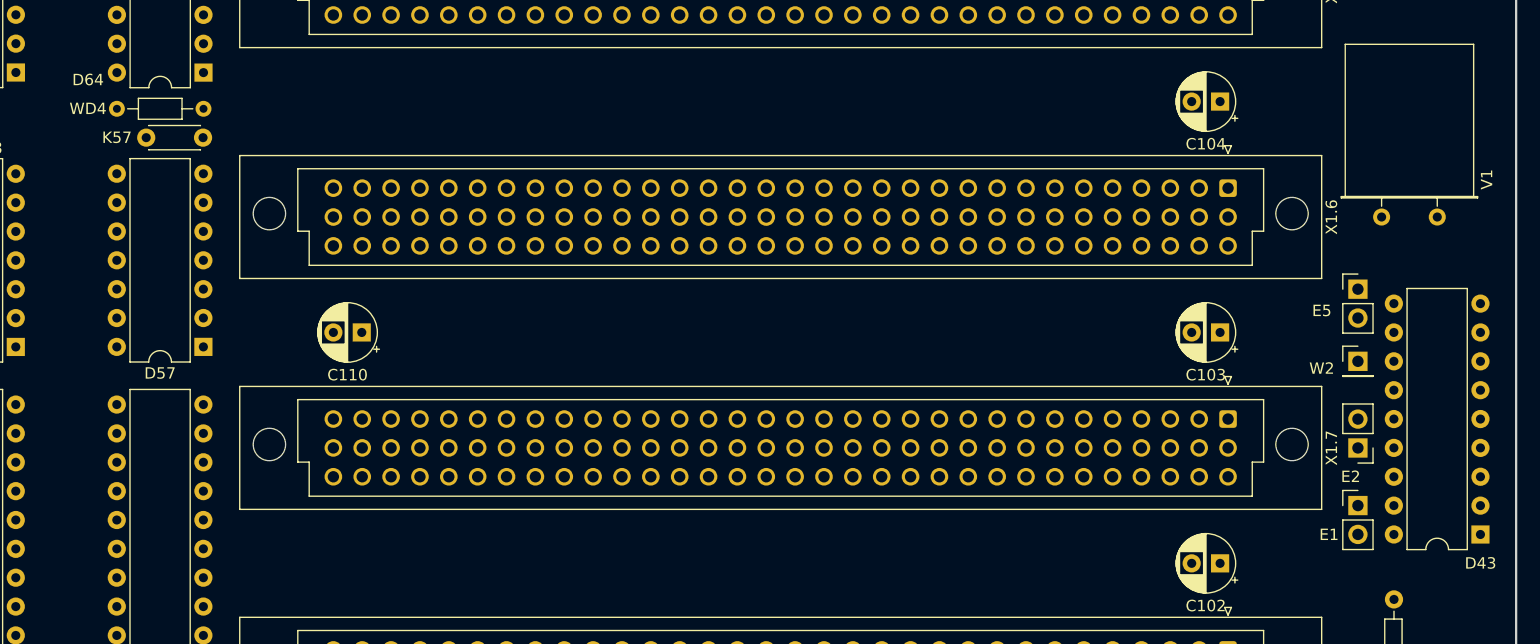
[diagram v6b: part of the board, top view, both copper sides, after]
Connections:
- D28 pad 1: (no net) -> GND
- D28 pad 2: (no net) -> /EC1834 201.1/XD0
- D28 pad 3: (no net) -> /EC1834 201.1/XD1
- D28 pad 4: (no net) -> /EC1834 201.1/XD2
- D28 pad 5: (no net) -> /EC1834 201.1/XD3
- D28 pad 6: (no net) -> +5V
- D28 pad 8: (no net) -> Net-(D28-Pad8)
- D28 pad 9: (no net) -> Net-(D28-Pad9)
- D29 pad 1: (no net) -> GND
- D29 pad 2: (no net) -> /EC1834 201.1/XD0
- D29 pad 3: (no net) -> /EC1834 201.1/XD1
- D29 pad 4: (no net) -> /EC1834 201.1/XD2
- D29 pad 5: (no net) -> /EC1834 201.1/XD3
- D29 pad 6: (no net) -> +5V
- D29 pad 8: (no net) -> Net-(D29-Pad8)
- D29 pad 9: (no net) -> Net-(D29-Pad9)
- D33 pad 10: Net-(D28-Pad08) -> Net-(D28-Pad8)
- D33 pad 13: Net-(D29-Pad08) -> Net-(D29-Pad8)
- D46 pad 1: (no net) -> /EC1834 201.1/AENBRD
- D46 pad 2: (no net) -> unconnected-(D46-Pad2)
- D46 pad 3: (no net) -> /EC1834 201.1/A0
- D46 pad 4: (no net) -> Net-(D46-Pad4)
- D46 pad 5: (no net) -> unconnected-(D46-Pad5)
- D46 pad 6: (no net) -> unconnected-(D46-Pad6)
- D46 pad 7: (no net) -> GND
- D46 pad 9: (no net) -> GND
- D55 pad 1: (no net) -> /EC1834 201.1/IRQ1
- D55 pad 2: (no net) -> Net-(C8-Pad1)
- D55 pad 3: (no net) -> unconnected-(D55-Pad3)
- D55 pad 4: (no net) -> unconnected-(D55-Pad4)
- D55 pad 5: (no net) -> unconnected-(D55-Pad5)
- D55 pad 6: (no net) -> unconnected-(D55-Pad6)
- D55 pad 7: (no net) -> unconnected-(D55-Pad7)
- D55 pad 8: (no net) -> unconnected-(D55-Pad8)
- D55 pad 9: (no net) -> unconnected-(D55-Pad9)
- D56 pad 1: (no net) -> Net-(D55-Pad32)
- D56 pad 2: (no net) -> Net-(D55-Pad31)
- D56 pad 3: (no net) -> Net-(D55-Pad30)
- D56 pad 4: (no net) -> Net-(D55-Pad29)
- D56 pad 5: (no net) -> Net-(D55-Pad28)
- D56 pad 6: (no net) -> Net-(D55-Pad27)
- D56 pad 7: (no net) -> Net-(D55-Pad26)
- D56 pad 8: (no net) -> Net-(D55-Pad25)
- D56 pad 9: (no net) -> /EC1834 201.2/0
- D6 pad 1: (no net) -> GND
- D6 pad 2: (no net) -> /EC1834 201.1/XD0
- D6 pad 3: (no net) -> /EC1834 201.1/XD1
- D6 pad 4: (no net) -> /EC1834 201.1/XD2
- D6 pad 5: (no net) -> /EC1834 201.1/XD3
- D6 pad 6: (no net) -> +5V
- D6 pad 8: (no net) -> Net-(D33-Pad4)
- D6 pad 9: (no net) -> Net-(D6-Pad9)
- D61 pad 1: (no net) -> Net-(D45-Pad9)
- D61 pad 2: (no net) -> unconnected-(D61-Pad2)
- D61 pad 3: (no net) -> unconnected-(D61-Pad3)
- D61 pad 4: (no net) -> GND
- D61 pad 5: (no net) -> unconnected-(D61-Pad5)
- D61 pad 6: (no net) -> unconnected-(D61-Pad6)
- D61 pad 7: (no net) -> GND
- D61 pad 9: (no net) -> GND
- D65 pad 1: (no net) -> /EC1834 201.1/A17
- D65 pad 2: (no net) -> /EC1834 201.1/A18
- D65 pad 3: (no net) -> /EC1834 201.1/A19
- D65 pad 4: (no net) -> Net-(D65-Pad4)
- D65 pad 5: (no net) -> /EC1834 201.2/PS4:2
- D65 pad 6: (no net) -> /EC1834 201.1/~{DACK0BRD}
- D65 pad 7: (no net) -> unconnected-(D65-Pad7)
- D65 pad 9: (no net) -> unconnected-(D65-Pad9)
- D66 pad 1: (no net) -> 5PW2
- D66 pad 2: (no net) -> /EC1834 201.1/A14
- D66 pad 3: (no net) -> 5PW2
- D66 pad 4: (no net) -> /EC1834 201.2/~{ROMADRSEL}
- D66 pad 5: (no net) -> /EC1834 201.1/~{XMEMR}
- D66 pad 6: (no net) -> /EC1834 201.1/~{RESETDRV}
- D66 pad 7: (no net) -> /EC1834 201.2/~{CSROM1}
- D66 pad 9: (no net) -> unconnected-(D66-Pad9)
- D7 pad 10: Net-(D46-Pad04) -> Net-(D46-Pad4)
- D7 pad 11: Net-(D46-Pad04) -> Net-(D46-Pad4)
- D8 pad 10: Net-(D29-Pad09) -> Net-(D29-Pad9)
- D8 pad 6: Net-(D6-Pad09) -> Net-(D6-Pad9)
- D8 pad 8: Net-(D28-Pad09) -> Net-(D28-Pad9)
- D89 pad 1: (no net) -> /EC1834 201.1/XA5
- D89 pad 2: (no net) -> /EC1834 201.1/XA6
- D89 pad 3: (no net) -> /EC1834 201.1/XA7
- D89 pad 4: (no net) -> /EC1834 201.1/XA8
- D89 pad 5: (no net) -> /EC1834 201.1/XA9
- D89 pad 6: (no net) -> /EC1834 201.1/~{AEN}
- D89 pad 7: (no net) -> Net-(D89-Pad7)
- D89 pad 9: (no net) -> /EC1834 201.1/~{INTRCS2}
- D9 pad 1: (no net) -> /EC1834 201.1/XA0
- D9 pad 2: (no net) -> /EC1834 201.1/XA1
- D9 pad 3: (no net) -> /EC1834 201.1/WRTDMAPGREG
- D9 pad 4: (no net) -> GND
- D9 pad 5: (no net) -> GND
- D9 pad 6: (no net) -> 5PW1
- D9 pad 7: (no net) -> Net-(D8-Pad5)
- D9 pad 9: (no net) -> Net-(D8-Pad11)
- R12 pad 5: Net-(D65-Pad04) -> Net-(D65-Pad4)
- W3 pad 1: Net-(D89-Pad07) -> Net-(D89-Pad7)
- WD4 pad 2: Net-(D65-Pad04) -> Net-(D65-Pad4)
- X1.1 pad b1: (no net) -> unconnected-(X1.1-Padb1)
- X1.1 pad b10: (no net) -> unconnected-(X1.1-Padb10)
- X1.1 pad b11: (no net) -> unconnected-(X1.1-Padb11)
- X1.1 pad b12: (no net) -> unconnected-(X1.1-Padb12)
- X1.1 pad b13: (no net) -> unconnected-(X1.1-Padb13)
- X1.1 pad b14: (no net) -> unconnected-(X1.1-Padb14)
- X1.1 pad b15: (no net) -> unconnected-(X1.1-Padb15)
- X1.1 pad b16: (no net) -> unconnected-(X1.1-Padb16)
- X1.1 pad b17: (no net) -> unconnected-(X1.1-Padb17)
- X1.1 pad b18: (no net) -> unconnected-(X1.1-Padb18)
- X1.1 pad b20: (no net) -> unconnected-(X1.1-Padb20)
- X1.1 pad b27: (no net) -> unconnected-(X1.1-Padb27)
- X1.1 pad b28: (no net) -> unconnected-(X1.1-Padb28)
- X1.1 pad b29: (no net) -> unconnected-(X1.1-Padb29)
- X1.1 pad b31: (no net) -> unconnected-(X1.1-Padb31)
- X1.2 pad b1: (no net) -> unconnected-(X1.2-Padb1)
- X1.2 pad b10: (no net) -> unconnected-(X1.2-Padb10)
- X1.2 pad b11: (no net) -> unconnected-(X1.2-Padb11)
- X1.2 pad b12: (no net) -> unconnected-(X1.2-Padb12)
- X1.2 pad b13: (no net) -> unconnected-(X1.2-Padb13)
- X1.2 pad b14: (no net) -> unconnected-(X1.2-Padb14)
- X1.2 pad b15: (no net) -> unconnected-(X1.2-Padb15)
- X1.2 pad b16: (no net) -> unconnected-(X1.2-Padb16)
- X1.2 pad b17: (no net) -> unconnected-(X1.2-Padb17)
- X1.2 pad b18: (no net) -> unconnected-(X1.2-Padb18)
- X1.2 pad b20: (no net) -> unconnected-(X1.2-Padb20)
- X1.2 pad b27: (no net) -> unconnected-(X1.2-Padb27)
- X1.2 pad b28: (no net) -> unconnected-(X1.2-Padb28)
- X1.2 pad b29: (no net) -> unconnected-(X1.2-Padb29)
- X1.2 pad b31: (no net) -> unconnected-(X1.2-Padb31)
- X1.3 pad b1: (no net) -> unconnected-(X1.3-Padb1)
- X1.3 pad b10: (no net) -> unconnected-(X1.3-Padb10)
- X1.3 pad b11: (no net) -> unconnected-(X1.3-Padb11)
- X1.3 pad b12: (no net) -> unconnected-(X1.3-Padb12)
- X1.3 pad b13: (no net) -> unconnected-(X1.3-Padb13)
- X1.3 pad b14: (no net) -> unconnected-(X1.3-Padb14)
- X1.3 pad b15: (no net) -> unconnected-(X1.3-Padb15)
- X1.3 pad b16: (no net) -> unconnected-(X1.3-Padb16)
- X1.3 pad b17: (no net) -> unconnected-(X1.3-Padb17)
- X1.3 pad b18: (no net) -> unconnected-(X1.3-Padb18)
- X1.3 pad b20: (no net) -> unconnected-(X1.3-Padb20)
- X1.3 pad b27: (no net) -> unconnected-(X1.3-Padb27)
- X1.3 pad b28: (no net) -> unconnected-(X1.3-Padb28)
- X1.3 pad b29: (no net) -> unconnected-(X1.3-Padb29)
- X1.3 pad b31: (no net) -> unconnected-(X1.3-Padb31)
- X1.4 pad b1: (no net) -> unconnected-(X1.4-Padb1)
- X1.4 pad b10: (no net) -> unconnected-(X1.4-Padb10)
- X1.4 pad b11: (no net) -> unconnected-(X1.4-Padb11)
- X1.4 pad b12: (no net) -> unconnected-(X1.4-Padb12)
- X1.4 pad b13: (no net) -> unconnected-(X1.4-Padb13)
- X1.4 pad b14: (no net) -> unconnected-(X1.4-Padb14)
- X1.4 pad b15: (no net) -> unconnected-(X1.4-Padb15)
- X1.4 pad b16: (no net) -> unconnected-(X1.4-Padb16)
- X1.4 pad b17: (no net) -> unconnected-(X1.4-Padb17)
- X1.4 pad b18: (no net) -> unconnected-(X1.4-Padb18)
- X1.4 pad b20: (no net) -> unconnected-(X1.4-Padb20)
- X1.4 pad b27: (no net) -> unconnected-(X1.4-Padb27)
- X1.4 pad b28: (no net) -> unconnected-(X1.4-Padb28)
- X1.4 pad b29: (no net) -> unconnected-(X1.4-Padb29)
- X1.4 pad b31: (no net) -> unconnected-(X1.4-Padb31)
- X1.5 pad b1: (no net) -> unconnected-(X1.5-Padb1)
- X1.5 pad b10: (no net) -> unconnected-(X1.5-Padb10)
- X1.5 pad b11: (no net) -> unconnected-(X1.5-Padb11)
- X1.5 pad b12: (no net) -> unconnected-(X1.5-Padb12)
- X1.5 pad b13: (no net) -> unconnected-(X1.5-Padb13)
- X1.5 pad b14: (no net) -> unconnected-(X1.5-Padb14)
- X1.5 pad b15: (no net) -> unconnected-(X1.5-Padb15)
- X1.5 pad b16: (no net) -> unconnected-(X1.5-Padb16)
- X1.5 pad b17: (no net) -> unconnected-(X1.5-Padb17)
- X1.5 pad b18: (no net) -> unconnected-(X1.5-Padb18)
- X1.5 pad b20: (no net) -> unconnected-(X1.5-Padb20)
- X1.5 pad b27: (no net) -> unconnected-(X1.5-Padb27)
- X1.5 pad b28: (no net) -> unconnected-(X1.5-Padb28)
- X1.5 pad b29: (no net) -> unconnected-(X1.5-Padb29)
- X1.5 pad b31: (no net) -> unconnected-(X1.5-Padb31)
- X1.6 pad b1: (no net) -> unconnected-(X1.6-Padb1)
- X1.6 pad b10: (no net) -> unconnected-(X1.6-Padb10)
- X1.6 pad b11: (no net) -> unconnected-(X1.6-Padb11)
- X1.6 pad b12: (no net) -> unconnected-(X1.6-Padb12)
- X1.6 pad b13: (no net) -> unconnected-(X1.6-Padb13)
- X1.6 pad b14: (no net) -> unconnected-(X1.6-Padb14)
- X1.6 pad b15: (no net) -> unconnected-(X1.6-Padb15)
- X1.6 pad b16: (no net) -> unconnected-(X1.6-Padb16)
- X1.6 pad b17: (no net) -> unconnected-(X1.6-Padb17)
- X1.6 pad b18: (no net) -> unconnected-(X1.6-Padb18)
- X1.6 pad b20: (no net) -> unconnected-(X1.6-Padb20)
- X1.6 pad b27: (no net) -> unconnected-(X1.6-Padb27)
- X1.6 pad b28: (no net) -> unconnected-(X1.6-Padb28)
- X1.6 pad b29: (no net) -> unconnected-(X1.6-Padb29)
- X1.6 pad b31: (no net) -> unconnected-(X1.6-Padb31)
- X1.7 pad b1: (no net) -> unconnected-(X1.7-Padb1)
- X1.7 pad b10: (no net) -> unconnected-(X1.7-Padb10)
- X1.7 pad b11: (no net) -> unconnected-(X1.7-Padb11)
- X1.7 pad b12: (no net) -> unconnected-(X1.7-Padb12)
- X1.7 pad b13: (no net) -> unconnected-(X1.7-Padb13)
- X1.7 pad b14: (no net) -> unconnected-(X1.7-Padb14)
- X1.7 pad b15: (no net) -> unconnected-(X1.7-Padb15)
- X1.7 pad b16: (no net) -> unconnected-(X1.7-Padb16)
- X1.7 pad b17: (no net) -> unconnected-(X1.7-Padb17)
- X1.7 pad b18: (no net) -> unconnected-(X1.7-Padb18)
- X1.7 pad b20: (no net) -> unconnected-(X1.7-Padb20)
- X1.7 pad b27: (no net) -> unconnected-(X1.7-Padb27)
- X1.7 pad b28: (no net) -> unconnected-(X1.7-Padb28)
- X1.7 pad b29: (no net) -> unconnected-(X1.7-Padb29)
- X1.7 pad b31: (no net) -> unconnected-(X1.7-Padb31)
- X1.8 pad b1: (no net) -> unconnected-(X1.8-Padb1)
- X1.8 pad b10: (no net) -> unconnected-(X1.8-Padb10)
- X1.8 pad b11: (no net) -> unconnected-(X1.8-Padb11)
- X1.8 pad b12: (no net) -> unconnected-(X1.8-Padb12)
- X1.8 pad b13: (no net) -> unconnected-(X1.8-Padb13)
- X1.8 pad b14: (no net) -> unconnected-(X1.8-Padb14)
- X1.8 pad b15: (no net) -> unconnected-(X1.8-Padb15)
- X1.8 pad b16: (no net) -> unconnected-(X1.8-Padb16)
- X1.8 pad b17: (no net) -> unconnected-(X1.8-Padb17)
- X1.8 pad b18: (no net) -> unconnected-(X1.8-Padb18)
- X1.8 pad b20: (no net) -> unconnected-(X1.8-Padb20)
- X1.8 pad b27: (no net) -> unconnected-(X1.8-Padb27)
- X1.8 pad b28: (no net) -> unconnected-(X1.8-Padb28)
- X1.8 pad b29: (no net) -> unconnected-(X1.8-Padb29)
- X1.8 pad b31: (no net) -> unconnected-(X1.8-Padb31)

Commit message: Wrong Signal fixed
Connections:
- D62 pad 4: /EC1834 201.1/XA9 -> /EC1834 201.1/XA8
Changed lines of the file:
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@@
       (net 283 "Net-(D45-Pad9)") (pinfunction "Y1") (pintype "output"))
     (pad "4" thru_hole oval (at 0 7.62 180) (size 1.6 1.6) (drill 0.8) (layers *.Cu *.Mask)
-      (net 416 "/EC1834 201.1/XA9") (pinfunction "A2") (pintype "input"))
+      (net 505 "/EC1834 201.1/XA8") (pinfunction "A2") (pintype "input"))
     (pad "5" thru_hole oval (at 0 10.16 180) (size 1.6 1.6) (drill 0.8) (layers *.Cu *.Mask)
       (net 416 "/EC1834 201.1/XA9") (pinfunction "B2") (pintype "input"))
